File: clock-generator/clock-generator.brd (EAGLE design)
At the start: 80 x 100 mm, 61 parts, among them IC1 24C00TS, U1 SN74LVC1G04DBV, U3 ATSAMD11-QFN24, U4 SI5351C, U5 IP4234CZ6, U6 IP4234CZ6, X1 MINI-USB-SHIELD-UX60A-MB-5ST, X2 JACK2.5_SJ-2523, X4 1-227161-0

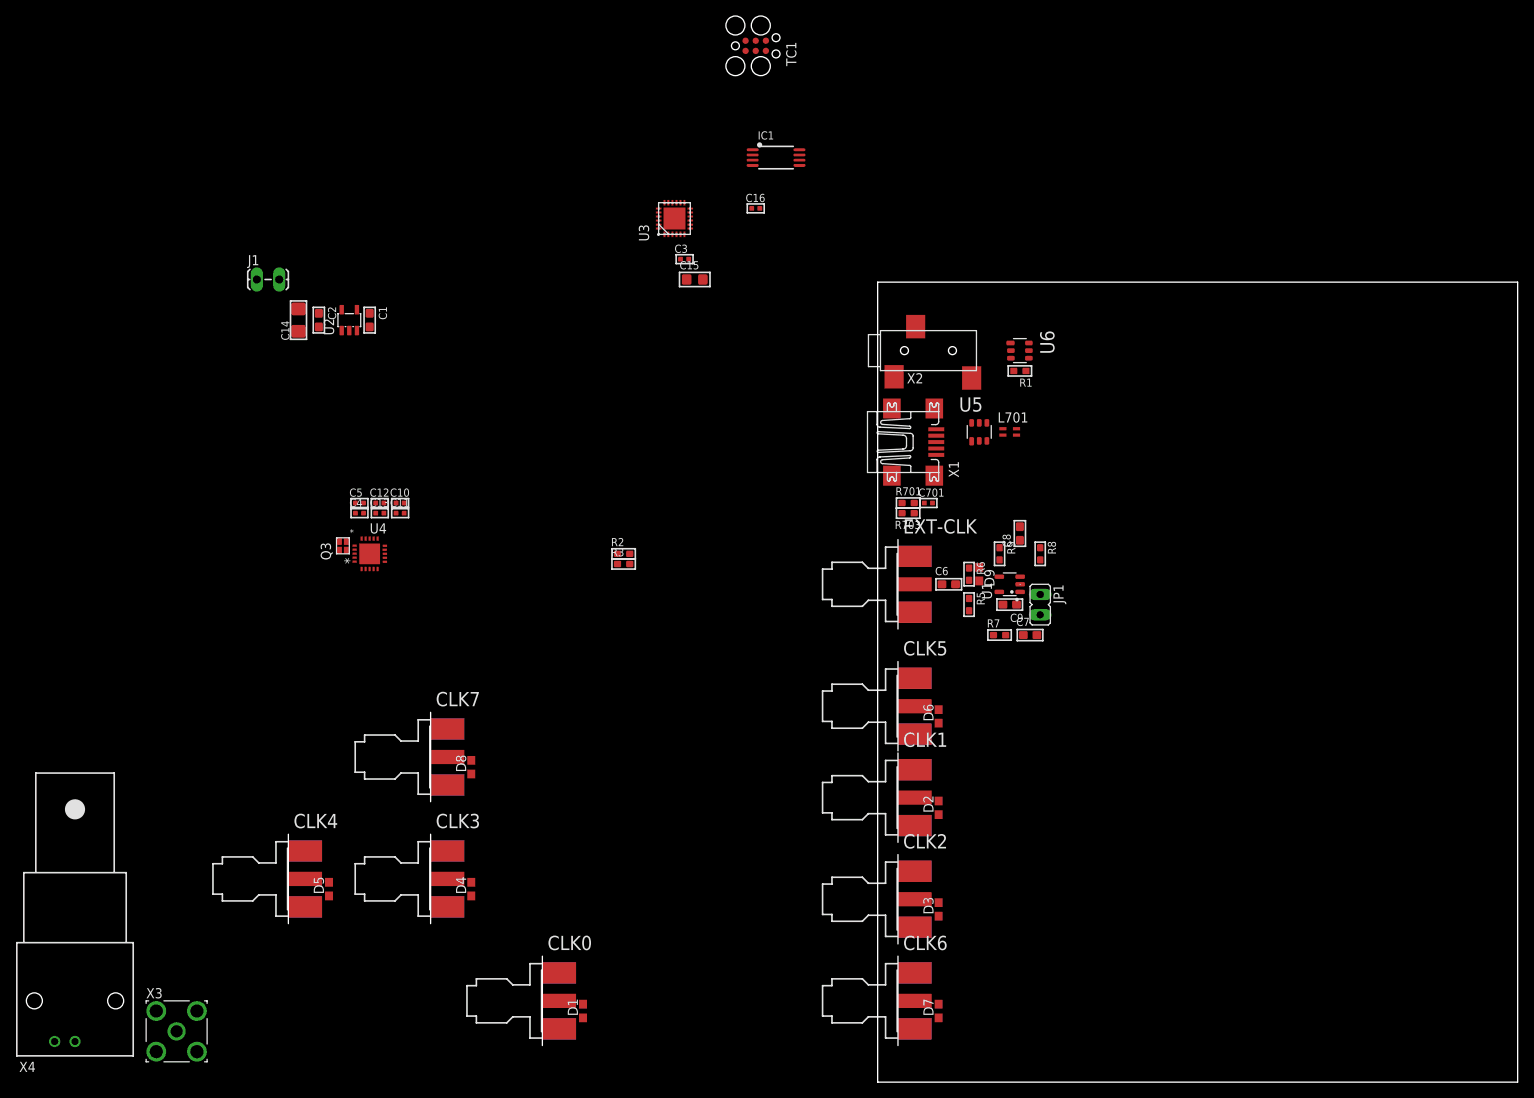
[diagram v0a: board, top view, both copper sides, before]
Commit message: clock-generator: Most of the layout
Traces are intended for dual-layer 1mm FR4 PCB with 35um copper.
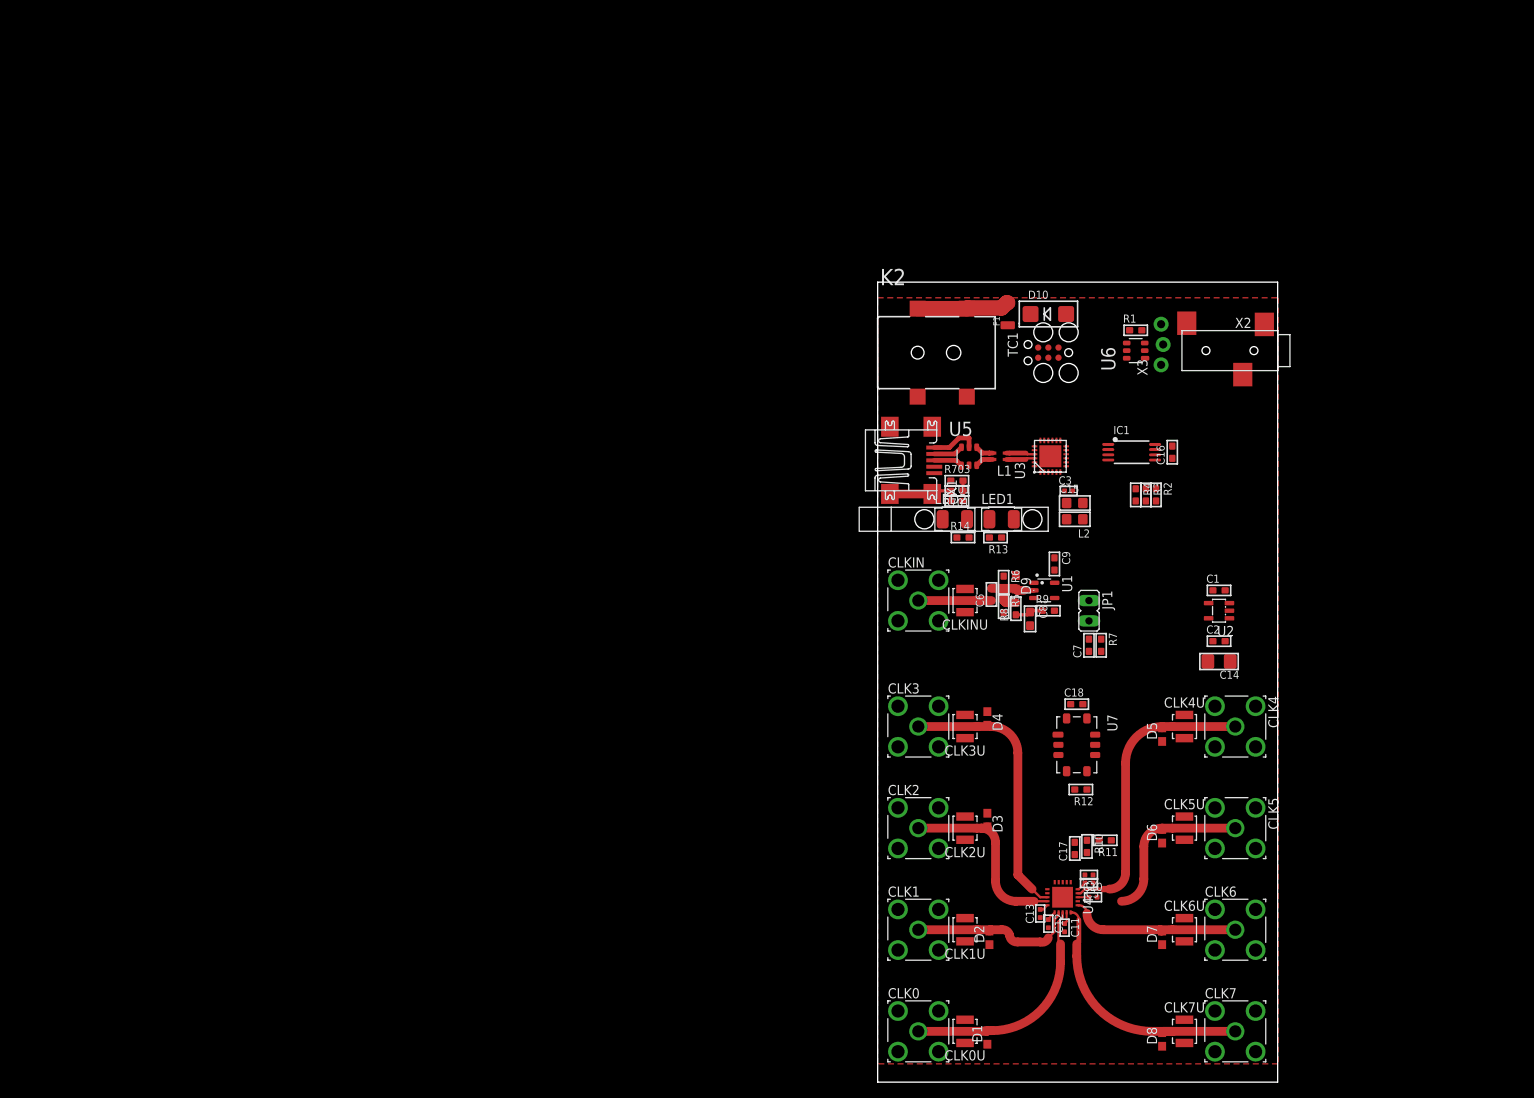
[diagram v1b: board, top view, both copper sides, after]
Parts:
- removed EXT-CLK: (no value), con-coax:J502-ND-142-0711-821/826
- removed J1: (no value), SparkFun-Connectors:1X02_LOCK_LONGPADS
- removed L701: 744231091, Wuerth_Elektronik_eiSos_V6_20140807:WE-CNSW_0805
- removed Q3: (no value), jackens:XO-SMD2X1.6X0.5MM
- removed X4: 1-227161-0, con-coax:AMP_227161
- added C17, C18: 100n, rc-sysmocom:_0603
- added CLK0U, CLK1U, CLK2U, CLK3U, CLK4U, CLK5U, CLK6U, CLK7U, CLKINU: (no value), laforge:HRS_UFL
- added CLKIN: (no value), laforge:SMA-F-S-TH
- added D10: DIODDE-ZENER-SMA, diodes-sysmocom:SMADIODE
- added F1: (no value), littlefuse:1206L
- added K2: 694108106102, Wurth_Elektronik_Electromechanic_DC_Power_Jack_Connectors_rev15c:694108106102
- added L1: 744231091, Wuerth_Elektronik_eiSos_V6_20140807:WE-CNSW_0805
- added L2: (no value), rc-sysmocom:_0805
- added LED1: green, LED-PLCC2:PLCC2-MIN
- added LED2: yellow, LED-PLCC2:PLCC2-MIN
- added M1: MENTOR_12701001, Mentor_lightpipe:1270.1001
- added R10, R11: 1k, rc-sysmocom:_0603
- added R12: 33, rc-sysmocom:_0603
- added R13, R14: 330, rc-sysmocom:_0603
- added R4: 10k, rc-sysmocom:_0603
- added U7: VCTCXO-CONNORWINFIELD, Connor-Winfield_VCTCXO:VCTCXO-CONNORWINFIELD
- C1, C2, C6, C7, C9: device rc-sysmocom:0603 -> rc-sysmocom:_0603
- C16, C701: device rc-sysmocom:_0402 -> rc-sysmocom:_0603
- CLK0: value SMA-142-0711-821/826 -> (none); device con-coax:J502-ND-142-0711-821/826 -> laforge:SMA-F-S-TH
- CLK1, CLK2, CLK3, CLK4, CLK5, CLK6, CLK7: device con-coax:J502-ND-142-0711-821/826 -> laforge:SMA-F-S-TH
- D1: value 0603ESDA-TR -> (none)
- R2, R3: value 2k2 -> 1k
- X3: device laforge:SMA-F-S-TH -> laforge:1X03_LOCK_NO_SILK
- moved X3 148.7 mm to (35.6, 89.7), turned to 90 degrees
- moved C14 122.7 mm to (42.7, 52.6), turned to 180 degrees
- moved CLK4 119.9 mm to (44.7, 44.5), turned to 270 degrees
- moved C2 119.5 mm to (42.7, 55.1), turned to 0 degrees
- moved U2 114.6 mm to (42.7, 58.9), turned to 90 degrees
- moved C1 111.4 mm to (42.7, 61.5), turned to 0 degrees
- moved CLK7 106.3 mm to (44.7, 6.35)
- moved D5 105.9 mm to (35.6, 43.4)
- moved C5 102.8 mm to (26.4, 24.9), turned to 180 degrees
- moved C4 101.8 mm to (26.4, 25.9), turned to 180 degrees
- moved C10 99.6 mm to (26.9, 23.1)
- moved C12 98.7 mm to (21.3, 19.8), turned to 270 degrees
- moved C11 97.9 mm to (23.4, 19.3), turned to 270 degrees
- moved U4 96.7 mm to (23.1, 23.1), turned to 270 degrees
- moved C13 96.5 mm to (20.3, 21.1), turned to 90 degrees
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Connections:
- removed net N$22: L701.2, U5.4
- removed net N$43: L701.3, U5.3
- removed net VIN: C1.2, J1.2, U2.1, U2.3
- removed net XB: Q3.1, U4.2
- new net !LED_YELLOW: LED2.K
- new net !OEB: U3.14, U4.7
- new net N$1: R11.1, R12.2
- new net N$10: U7.10
- new net N$11: LED1.A, R13.1
- new net N$12: LED2.A, R14.1
- new net N$13: C15.2, C3.2, L2.1, U3.24
- new net N$14: C1.2, D10.C, F1.1, U2.1, U2.3
- new net N$15: F1.2, K2.1, K2.1-1
- new net N$2: C17.2, R10.1, R11.2
- new net N$4: R12.1, U7.5
- new net N$9: C18.2, U7.9
- new net USB1_D_N: L1.3, U5.4
- new net USB1_D_P: L1.2, U5.3
- new net VCTCXO_EN: U7.8
- net !INT: now also R4.2
- net CLK0_LINE: now also CLK0.C, CLK0U.SIG; no longer CLK0.1
- net CLK1_LINE: now also CLK1.C, CLK1U.SIG; no longer CLK1.1
- net CLK2_LINE: now also CLK2.C, CLK2U.SIG; no longer CLK2.1
- net CLK3_LINE: now also CLK3.C, CLK3U.SIG; no longer CLK3.1
- net CLK4_LINE: now also CLK4.C, CLK4U.SIG; no longer CLK4.1
- net CLK5_LINE: now also CLK5.C, CLK5U.SIG; no longer CLK5.1
- net CLK6_LINE: now also CLK6.C, CLK6U.SIG; no longer CLK6.1
- net CLK7_LINE: now also CLK7.C, CLK7U.SIG; no longer CLK7.1
- net CLKIN: now also CLKIN.C, CLKINU.SIG; no longer EXT-CLK.1
- net GND: now also C18.1, CLK0.G1, CLK0.G2, CLK0.G3, CLK0.G4, CLK0U.GND@1, CLK0U.GND@2, CLK1.G1, CLK1.G2, CLK1.G3, CLK1.G4, CLK1U.GND@1, CLK1U.GND@2, CLK2.G1, CLK2.G2, CLK2.G3, CLK2.G4, CLK2U.GND@1, CLK2U.GND@2, CLK3.G1, CLK3.G2, CLK3.G3, CLK3.G4, CLK3U.GND@1, CLK3U.GND@2, CLK4.G1, CLK4.G2, CLK4.G3, CLK4.G4, CLK4U.GND@1, CLK4U.GND@2, CLK5.G1, CLK5.G2, CLK5.G3, CLK5.G4, CLK5U.GND@1, CLK5U.GND@2, CLK6.G1, CLK6.G2, CLK6.G3, CLK6.G4, CLK6U.GND@1, CLK6U.GND@2, CLK7.G1, CLK7.G2, CLK7.G3, CLK7.G4, CLK7U.GND@1, CLK7U.GND@2, CLKIN.G1, CLKIN.G2, CLKIN.G3, CLKIN.G4, CLKINU.GND@1, CLKINU.GND@2, D10.A, IC1.1, IC1.2, IC1.3, K2.2, K2.3, LED1.K, R10.2, U7.4, X3.1; no longer CLK0.G@1, CLK0.G@2, CLK0.G@3, CLK0.G@4, CLK1.G@1, CLK1.G@2, CLK1.G@3, CLK1.G@4, CLK2.G@1, CLK2.G@2, CLK2.G@3, CLK2.G@4, CLK3.G@1, CLK3.G@2, CLK3.G@3, CLK3.G@4, CLK4.G@1, CLK4.G@2, CLK4.G@3, CLK4.G@4, CLK5.G@1, CLK5.G@2, CLK5.G@3, CLK5.G@4, CLK6.G@1, CLK6.G@2, CLK6.G@3, CLK6.G@4, CLK7.G@1, CLK7.G@2, CLK7.G@3, CLK7.G@4, EXT-CLK.G@1, EXT-CLK.G@2, EXT-CLK.G@3, EXT-CLK.G@4, J1.1, U4.7, X3.G1, X3.G2, X3.G3, X3.G4
- net N$6: now also X3.3
- net N$8: now also X3.2
- net USB_D_N: now also L1.4; no longer L701.1
- net USB_D_P: now also L1.1; no longer L701.4
- net VDD: now also L2.2, R13.2, R14.2, R4.1; no longer C15.2, C3.2, U3.24
- net XA: now also C17.1; no longer Q3.3
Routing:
- net CLK4_LINE: track 0.00 -> 36.5 mm
- net CLK3_LINE: track 0.00 -> 33.9 mm
- net CLK7_LINE: track 0.00 -> 31.1 mm
- net CLK0_LINE: track 0.00 -> 27.9 mm
- net CLK2_LINE: track 0.00 -> 23.6 mm
- net CLK6_LINE: track 0.00 -> 21.3 mm
- net CLK1_LINE: track 0.00 -> 20.8 mm
- net CLK5_LINE: track 0.00 -> 20.6 mm
- net N$15: track 0.00 -> 11.6 mm
- net CLKIN: track 0.00 -> 9.14 mm
- net N$61: track 0.00 -> 9.05 mm
- net CLKIN_AC: track 0.00 -> 8.56 mm
- net VDD: track 0.00 -> 6.48 mm
- net VBUS: track 0.00 -> 6.01 mm
- net USB0_D_N: track 0.00 -> 3.75 mm
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- added copper zone on layer 1, net GND
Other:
- board size 80 x 100 mm -> 50 x 100 mm

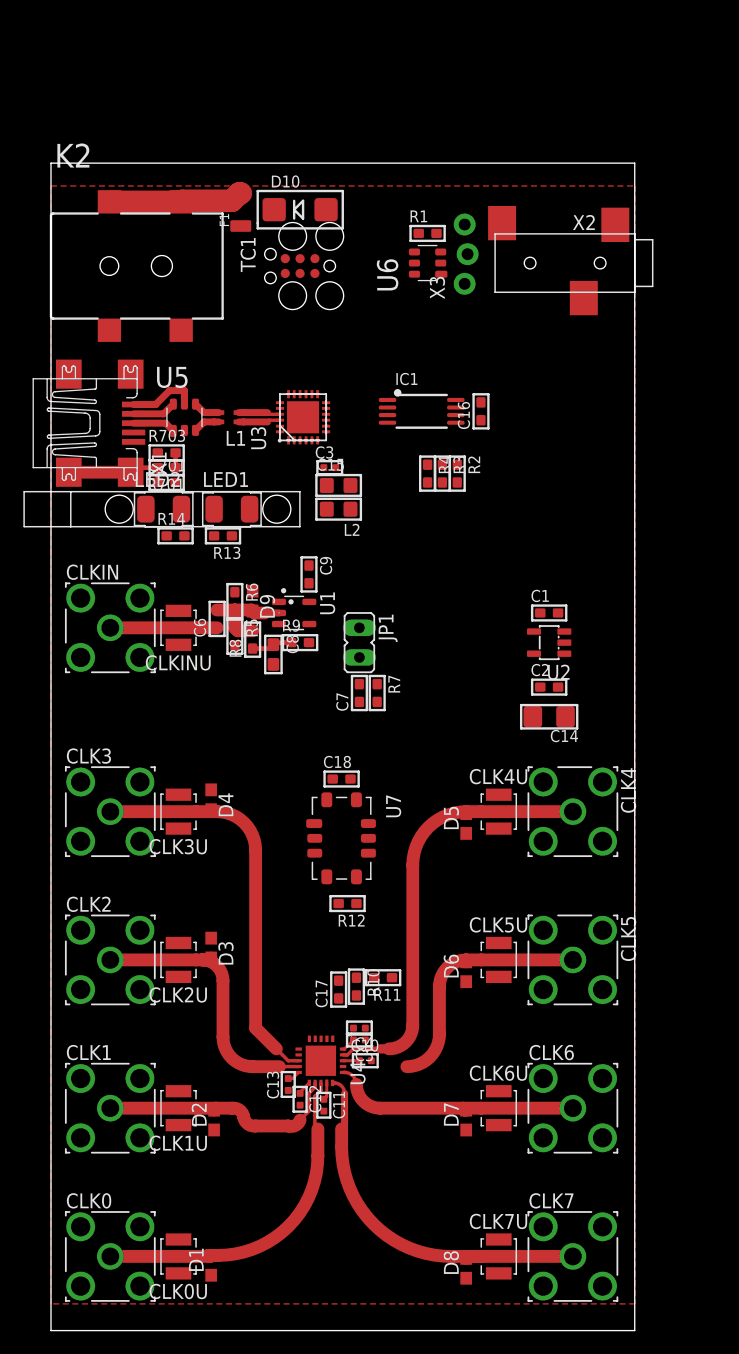
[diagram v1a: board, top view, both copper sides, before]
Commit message: clock-gen: Add SPI; UEXT header; mounting holes; do layout/routing
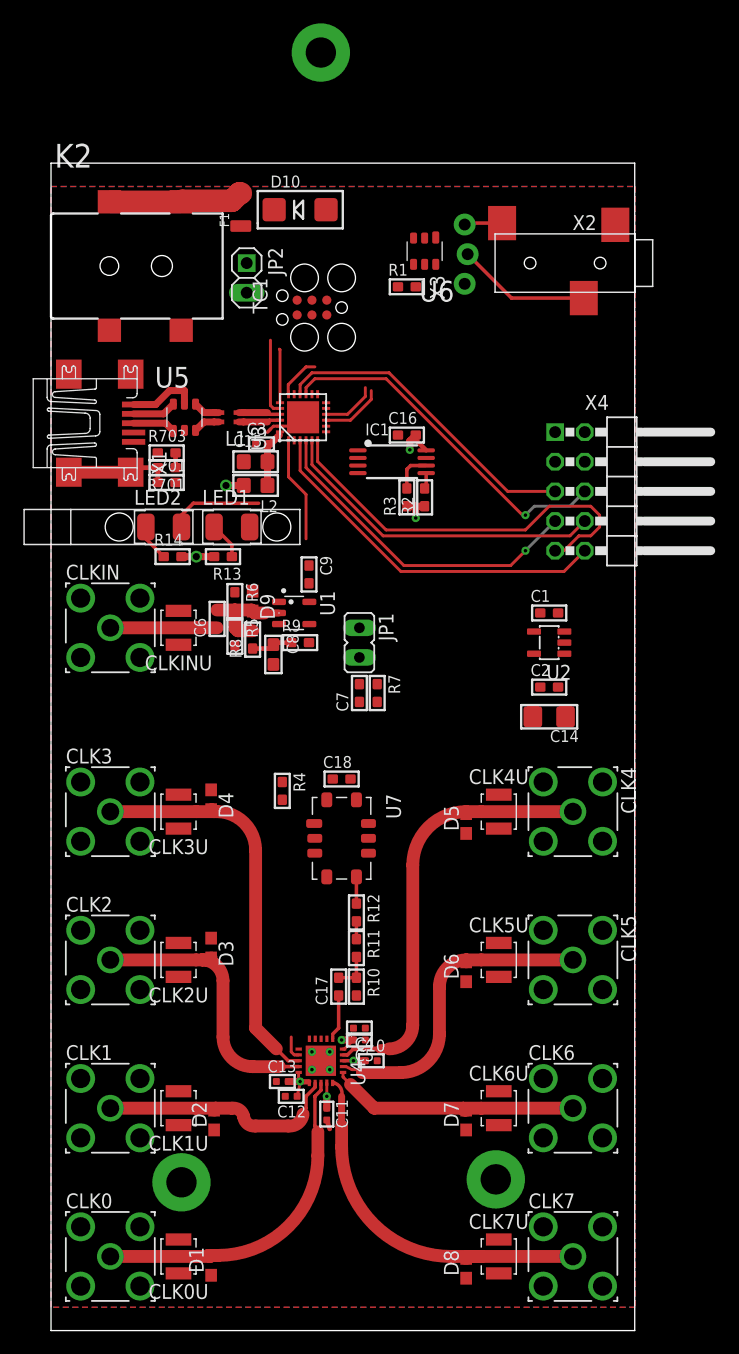
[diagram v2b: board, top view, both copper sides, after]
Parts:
- added JP2: (no value), laforge:1X02
- added X4: UEXT/90, laforge:2X05/90
- moved R4 29.9 mm to (19.8, 46.2)
- moved C15 7.40 mm to (17.5, 74.4)
- moved L2 7.40 mm to (17.5, 72.4)
- moved C16 6.67 mm to (30.5, 76.7), turned to 0 degrees
- moved C3 6.19 mm to (18.0, 75.9)
- moved IC1 5.01 mm to (29.2, 74.4)
- moved R1 4.91 mm to (30.5, 89.4)
- moved TC1 3.70 mm to (22.4, 87.6)
- moved R3 3.66 mm to (30.5, 71.4), turned to 90 degrees
- moved R2 3.45 mm to (32.0, 71.4), turned to 90 degrees
- moved R11 3.42 mm to (26.2, 32.8), turned to 270 degrees
- moved R14 1.80 mm to (10.4, 66.3)
- moved R13 1.78 mm to (14.7, 66.3)
- moved LED1 1.52 mm to (15.5, 68.8)
- moved LED2 1.52 mm to (9.65, 68.8)
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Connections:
- new net !SPI_SS: U3.3, X4.10
- new net SPI_MISO: U3.4, X4.7
- new net SPI_MOSI: U3.5, X4.8
- new net SPI_SCK: U3.6, X4.9
- net !LED_YELLOW: now also U3.13
- net GND: now also JP2.2, X4.2
- net I2C_SCL: now also X4.5
- net I2C_SDA: now also X4.6
- net N$15: now also JP2.1
- net SWCLK: now also TC1.6; no longer TC1.5
- net SWDIO: now also TC1.5; no longer TC1.6
- net UART_RX: now also X4.4
- net UART_TX: now also X4.3
- net VDD: now also X4.1
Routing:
- net SPI_SCK: track 0.00 -> 35.2 mm
- net I2C_SDA: track 0.00 -> 31.8 mm, vias 0 -> 1
- net !SPI_SS: track 0.00 -> 31.3 mm
- net I2C_SCL: track 0.00 -> 30.7 mm
- net SPI_MISO: track 0.00 -> 28.7 mm, vias 0 -> 1
- net SPI_MOSI: track 0.00 -> 28.5 mm
- net VDD: track 6.48 -> 23.1 mm, vias 0 -> 8
- net N$8: track 0.00 -> 11.5 mm
- net !INT: track 0.00 -> 9.06 mm
- net !LED_YELLOW: track 0.00 -> 8.04 mm
- net SWDIO: track 0.00 -> 6.51 mm
- net CLK5_LINE: track 20.6 -> 26.4 mm
- net UART_TX: track 0.00 -> 5.37 mm
- net N$13: track 0.00 -> 5.19 mm
- net UART_RX: track 0.00 -> 4.75 mm
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- added copper zone on layer 16, net VDD

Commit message: clock-gen: Connect EEPROM WP to GND to disable write-protect
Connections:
- net GND: now also IC1.7
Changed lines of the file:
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@@
 <wire x1="20.828" y1="77.47" x2="21.59" y2="78.232" width="0.254" layer="1"/>
 <wire x1="23.622" y1="18.034" x2="23.876" y2="17.272" width="0.4064" layer="1"/>
+<contactref element="IC1" pad="7"/>
 <wire x1="23.5585" y1="96.012" x2="23.114" y2="109.474" width="0" layer="19" extent="1-1"/>
 <wire x1="23.876" y1="23.876" x2="26.924" y2="24.892" width="0" layer="19" extent="1-1"/>
@@
 <wire x1="22.352" y1="22.352" x2="23.114" y2="23.114" width="0" layer="19" extent="1-1"/>
 <wire x1="26.285" y1="75.397" x2="21.59" y2="78.232" width="0" layer="19" extent="1-1"/>
+<wire x1="32.135" y1="74.747" x2="29.718" y2="76.708" width="0" layer="19" extent="1-1"/>
 <wire x1="22.352" y1="88.265" x2="16.764" y2="88.9" width="0" layer="19" extent="1-1"/>
 </signal>
